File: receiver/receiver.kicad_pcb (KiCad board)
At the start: 2 copper layers, 71.4 x 53.5 mm, 42 parts, among them CON1 AVR-ISP-6, IC1 ATTINY441-SSU, P1 LASER, P2 BATTERY, P3 CONN_01X01, P4 CONN_01X01, Q1 OPTO_NPN, Q2 OPTO_NPN, Q3 OPTO_NPN, Q4 OPTO_NPN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

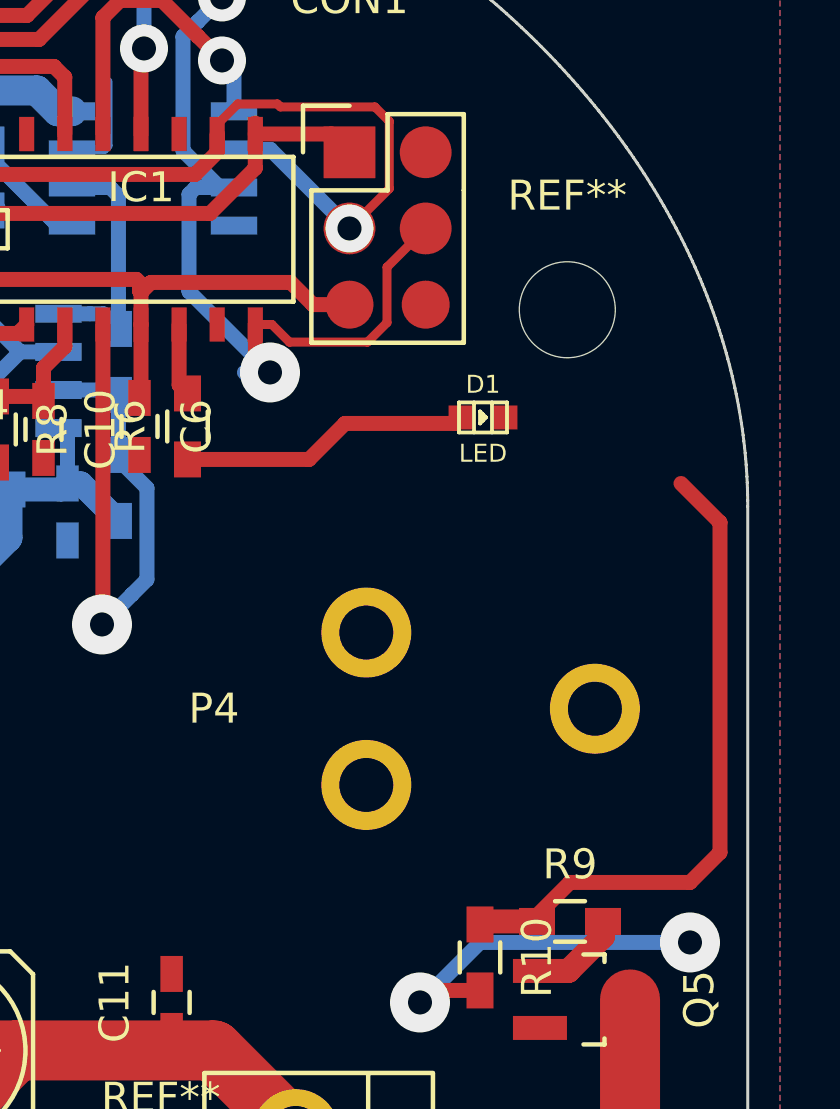
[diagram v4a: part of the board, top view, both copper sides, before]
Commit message: Put LED to place, connect the laser on line
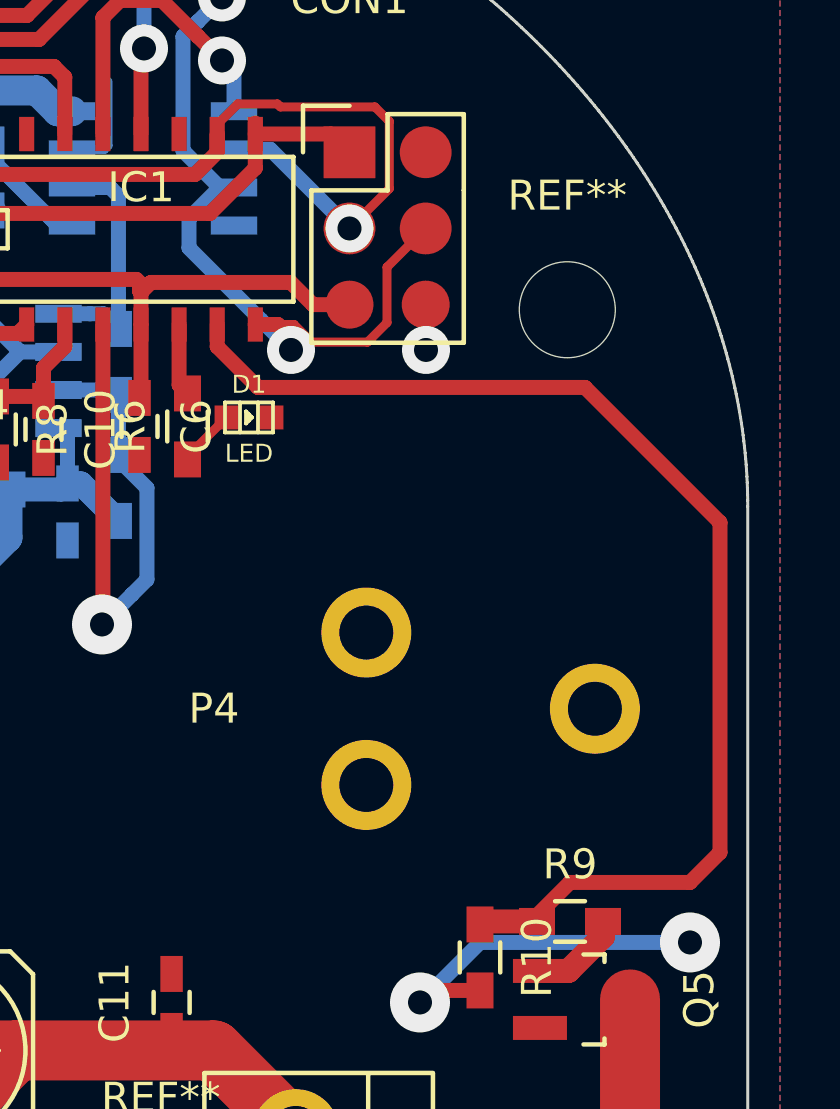
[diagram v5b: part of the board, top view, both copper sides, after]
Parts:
- moved D1 7.80 mm to (106.3, 103.5)
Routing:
- net /LASER_ON: track 22.3 -> 40.4 mm
- net Net-(D1-Pad1): track 9.71 -> 1.94 mm
- net /MOSI: track 52.9 -> 50.6 mm
- net GND: track 73.4 -> 74.9 mm, vias 12 -> 13
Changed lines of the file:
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@@
     (links 92)
     (no_connects 1)
-    (area 51.439999 80.438651 122.974692 134.024753)
+    (area 44.881429 80 129.538572 134.855)
     (thickness 1.6)
     (drawings 467)
-    (tracks 337)
+    (tracks 340)
     (zones 0)
     (modules 42)
@@
   )
   (setup
-    (last_trace_width 1)
+    (last_trace_width 0.3)
     (user_trace_width 0.3)
     (user_trace_width 0.5)
@@
     (pad_to_mask_clearance 0.2)
     (aux_axis_origin 0 0)
-    (visible_elements FFFE6E79)
+    (visible_elements FFFEEE79)
     (pcbplotparams
       (layerselection 0x00030_ffffffff)
@@
   )
   (module w_smd_leds:Led_0603 (layer F.Cu)
-    (at 114.1 103.5)
+    (at 106.3 103.5)
     (descr "SMD LED, 0603")
     (fp_text reference D1 (at 0 -1.09982) (layer F.SilkS)
@@
   (segment (start 98.24902 107.49944) (end 88.79944 116.94902) (width 1) (layer B.Cu) (net 1))
   (segment (start 88.79944 116.94902) (end 87.2 116.94902) (width 1) (layer B.Cu) (net 1))
+  (segment (start 112.19 101.23999) (end 112.2 101.24999) (width 0.3) (layer F.Cu) (net 2))
+  (via (at 112.2 101.24999) (size 1.6) (drill 0.8) (layers F.Cu B.Cu) (net 2))
+  (segment (start 112.19 99.74) (end 112.19 101.23999) (width 0.3) (layer F.Cu) (net 2))
   (segment (start 72.8 106.5) (end 72.8 107.2) (width 0.5) (layer F.Cu) (net 2))
   (segment (start 72.8 107.2) (end 74.7 109.1) (width 0.5) (layer F.Cu) (net 2))
@@
   (segment (start 99.45 101.85) (end 100.16 101.14) (width 0.5) (layer F.Cu) (net 6))
   (segment (start 100.16 101.14) (end 100.16 100.402) (width 0.5) (layer F.Cu) (net 6))
-  (segment (start 113.2 103.7) (end 113.3507 103.5493) (width 0.5) (layer F.Cu) (net 7))
-  (segment (start 113.3507 103.5493) (end 113.3507 103.5) (width 0.5) (layer F.Cu) (net 7))
-  (segment (start 104.25 104.9) (end 108.3 104.9) (width 0.5) (layer F.Cu) (net 7))
-  (segment (start 108.3 104.9) (end 109.5 103.7) (width 0.5) (layer F.Cu) (net 7))
-  (segment (start 109.5 103.7) (end 113.2 103.7) (width 0.5) (layer F.Cu) (net 7))
+  (segment (start 104.25 104.9) (end 104.25 104.8007) (width 0.3) (layer F.Cu) (net 7))
+  (segment (start 104.25 104.8007) (end 105.5507 103.5) (width 0.3) (layer F.Cu) (net 7))
   (segment (start 101.43 110.370008) (end 101.4 110.400008) (width 0.5) (layer F.Cu) (net 8))
   (segment (start 102.399999 109.400009) (end 101.4 110.400008) (width 0.5) (layer B.Cu) (net 8))
@@
   (via (at 109.65 97.2) (size 1.6) (drill 0.8) (layers F.Cu B.Cu) (net 18))
   (segment (start 105.24 94.052) (end 105.24 94.597502) (width 0.5) (layer F.Cu) (net 18))
-  (segment (start 104.3 99.3) (end 107 102) (width 0.5) (layer B.Cu) (net 19))
-  (segment (start 105.8 95.835) (end 104.525 95.835) (width 0.5) (layer B.Cu) (net 19))
-  (segment (start 104.525 95.835) (end 104.3 96.06) (width 0.5) (layer B.Cu) (net 19))
-  (segment (start 104.3 96.06) (end 104.3 99.3) (width 0.5) (layer B.Cu) (net 19))
+  (segment (start 106.700001 100.249991) (end 107.7 101.24999) (width 0.5) (layer B.Cu) (net 19))
+  (segment (start 107.264 100.402) (end 107.7 100.838) (width 0.5) (layer F.Cu) (net 19))
+  (via (at 107.7 101.24999) (size 1.6) (drill 0.8) (layers F.Cu B.Cu) (net 19))
+  (segment (start 104.3 97.84999) (end 106.700001 100.249991) (width 0.5) (layer B.Cu) (net 19))
+  (segment (start 106.51 100.402) (end 107.264 100.402) (width 0.5) (layer F.Cu) (net 19))
+  (segment (start 107.7 100.838) (end 107.7 101.24999) (width 0.5) (layer F.Cu) (net 19))
+  (segment (start 105.325 95.835) (end 104.3 96.86) (width 0.5) (layer B.Cu) (net 19))
+  (segment (start 104.3 96.86) (end 104.3 97.84999) (width 0.5) (layer B.Cu) (net 19))
   (segment (start 105.8 95.835) (end 105.325 95.835) (width 0.5) (layer B.Cu) (net 19))
+  (segment (start 112.19 97.2) (end 110.900001 98.489999) (width 0.3) (layer F.Cu) (net 19))
+  (segment (start 110.250001 100.990001) (end 108.390001 100.990001) (width 0.3) (layer F.Cu) (net 19))
+  (segment (start 110.900001 98.489999) (end 110.900001 100.340001) (width 0.3) (layer F.Cu) (net 19))
+  (segment (start 110.900001 100.340001) (end 110.250001 100.990001) (width 0.3) (layer F.Cu) (net 19))
+  (segment (start 108.390001 100.990001) (end 107.802 100.402) (width 0.3) (layer F.Cu) (net 19))
+  (segment (start 107.802 100.402) (end 106.51 100.402) (width 0.3) (layer F.Cu) (net 19))
   (segment (start 83.1 93.6) (end 86.389964 93.6) (width 0.5) (layer F.Cu) (net 19))
   (segment (start 86.389964 93.6) (end 89.7 90.289964) (width 0.5) (layer F.Cu) (net 19))
@@
   (segment (start 104.1 94.61) (end 104.1 90.8) (width 0.5) (layer B.Cu) (net 19))
   (via (at 105.4 89.5) (size 1.6) (drill 0.8) (layers F.Cu B.Cu) (net 19))
-  (segment (start 106.148026 102) (end 107 102) (width 0.5) (layer B.Cu) (net 19))
-  (segment (start 106.51 101.51) (end 107 102) (width 0.5) (layer F.Cu) (net 19))
-  (segment (start 106.51 100.402) (end 106.51 101.51) (width 0.5) (layer F.Cu) (net 19))
-  (via (at 107 102) (size 2) (drill 0.8) (layers F.Cu B.Cu) (net 19))
-  (segment (start 112.19 97.2) (end 110.900001 98.489999) (width 0.3) (layer F.Cu) (net 19))
-  (segment (start 110.900001 98.489999) (end 110.900001 100.340001) (width 0.3) (layer F.Cu) (net 19))
-  (segment (start 110.900001 100.340001) (end 110.250001 100.990001) (width 0.3) (layer F.Cu) (net 19))
-  (segment (start 110.250001 100.990001) (end 107.652001 100.990001) (width 0.3) (layer F.Cu) (net 19))
-  (segment (start 107.652001 100.990001) (end 107.064 100.402) (width 0.3) (layer F.Cu) (net 19))
-  (segment (start 107.064 100.402) (end 106.51 100.402) (width 0.3) (layer F.Cu) (net 19))
+  (segment (start 122 118) (end 122 107) (width 0.5) (layer F.Cu) (net 20))
+  (segment (start 115.9 120.3) (end 115.9 120.1) (width 0.5) (layer F.Cu) (net 20))
+  (segment (start 121 119) (end 122 118) (width 0.5) (layer F.Cu) (net 20))
+  (segment (start 106.6 102.5) (end 105.24 101.14) (width 0.5) (layer F.Cu) (net 20))
+  (segment (start 115.9 120.1) (end 117 119) (width 0.5) (layer F.Cu) (net 20))
+  (segment (start 117 119) (end 121 119) (width 0.5) (layer F.Cu) (net 20))
+  (segment (start 122 107) (end 117.5 102.5) (width 0.5) (layer F.Cu) (net 20))
+  (segment (start 117.5 102.5) (end 106.6 102.5) (width 0.5) (layer F.Cu) (net 20))
+  (segment (start 105.24 101.14) (end 105.24 100.402) (width 0.5) (layer F.Cu) (net 20))
   (segment (start 105.24 100.402) (end 105.24 100.0845) (width 0.25) (layer F.Cu) (net 20))
-  (segment (start 120.7 105.7) (end 122 107) (width 0.5) (layer F.Cu) (net 20))
-  (segment (start 122 107) (end 122 118) (width 0.5) (layer F.Cu) (net 20))
-  (segment (start 122 118) (end 121 119) (width 0.5) (layer F.Cu) (net 20))
-  (segment (start 121 119) (end 117 119) (width 0.5) (layer F.Cu) (net 20))
-  (segment (start 117 119) (end 115.9 120.1) (width 0.5) (layer F.Cu) (net 20))
-  (segment (start 115.9 120.1) (end 115.9 120.3) (width 0.5) (layer F.Cu) (net 20))
   (segment (start 115.9 120.3) (end 114.1 120.3) (width 0.8) (layer F.Cu) (net 20))
   (segment (start 114.1 120.3) (end 114 120.4) (width 0.8) (layer F.Cu) (net 20))
